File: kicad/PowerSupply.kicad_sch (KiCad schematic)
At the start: 49 parts, among them Q1 FQP17P10, Q2 FQP17P10, Q3 2N7002NXAK, Q4 2N7002NXAK, U1 AS324, U2 TLV197

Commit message: Changes
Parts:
- removed C4: 100nF, Capacitor_SMD:C_0805_2012Metric_Pad1.15x1.40mm_HandSolder, symbol Device:C_Small
- removed R8: ?, symbol Device:R
- added C?: 100n, symbol Device:C_Small
- added D?: D, symbol Device:D
- added D?: 10V, symbol Device:D_Zener
- added R?: 10k, symbol Device:R
- D1, D2: value 10V-16V -> 10V
- R15: value 100K -> 10K
- U1: MPN AS324MTR-G1 -> OPA4196IDR
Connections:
- net GND: now also C3.1; no longer R3.2
- net GNDA: now also R3.2, C?.2
- net Iread: now also C?.1, R?.2; no longer R4.2, U2.6
- net SVOUT: now also D?.1 (K)
- net VOUT+: now also D?.1 (K)
- net at R9.2: now also R6.2, U1.1
- net at R1.1, R2.2, R23.1: now also D?.2 (A)
- net at Q1.1 (G), Q2.1 (G), R5.1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: now also D?.2 (A)
- new net: R4.2, R?.1, U2.6
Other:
- moved on the sheet: C3, R1, R2, R3, R4, U2

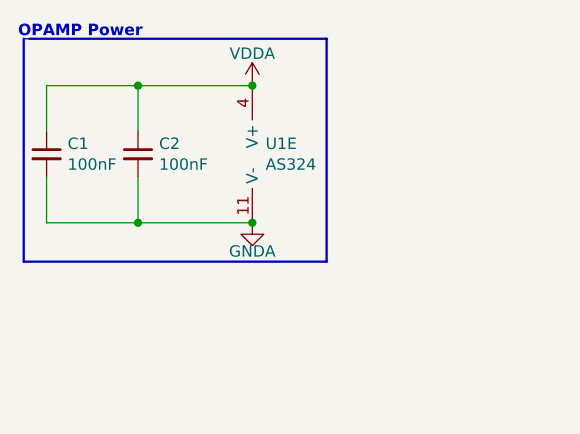
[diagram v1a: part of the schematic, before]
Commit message: Updated files to kicad 8
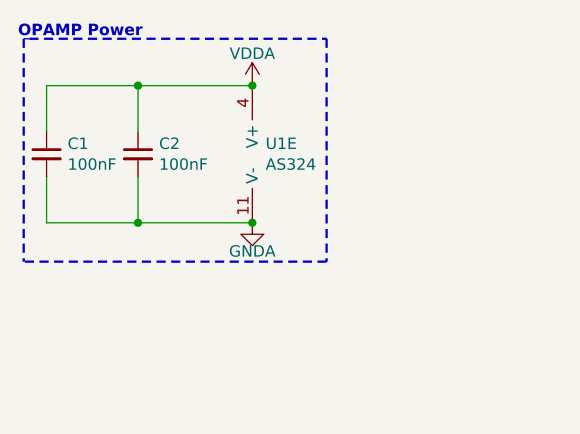
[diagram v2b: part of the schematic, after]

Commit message: Fixed a bunch of alignment
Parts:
- gave numbers to parts that had none: 4
- renumbered D1 to D2, D2 to D3, R5 to R6, R6 to R7, R7 to R8
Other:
- moved on the sheet: C1, C2, C3, C4, C7, D1, D2, D3, Q1, Q2, Q3, Q4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
